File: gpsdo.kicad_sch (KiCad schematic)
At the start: 213 parts, among them J1 OLED, J10 10MHZ_OUT, J11 100MHZ_OUT, J12 10MHZ_OUT, J13 10MHZ_OUT, J14 10MHZ_OUT, J15 10MHZ_OUT, J16 LED, J17 TIMEPULSE, J18 USB_DM, J19 USB_DP, J2 ARDUINO_UART, J20 SDA, J21 SCL, J22 FREQ0, J23 BOOT, J24 RESET, J25 D_SEL, J26 Freq Out, J27 VCC_OUT, J28 VDD_USB, J29 V_ANT, J3 VOLTMETER, J4 ARDUINO_EXTRA_PINS, J5 POWER_IN, J6 GPS_ANT, J7 10MHZ_OUT, J8 10MHZ_OUT, J9 10MHZ_OUT, U1 TPS79301-EP, U10 MSA-0385, U11 MSA-0385, U12 MSA-0385, U13 MSA-0385, U14 MSA-0385, U15 MSA-0385, U16 MSA-0385, U17 MSA-0385, U18 MSA-0385, U19 MSA-0385, U2 TPS79301-EP, U20 MSA-0385, U21 TPS7A4501DCQT, U3 TPS7A4501DCQT, U4 SN74HC541DWR, U5 DAC8571IDGKR, U6 LEA-M8F, U7 CVSS-945, U8 SN74HC541DWR, U9 MC12080

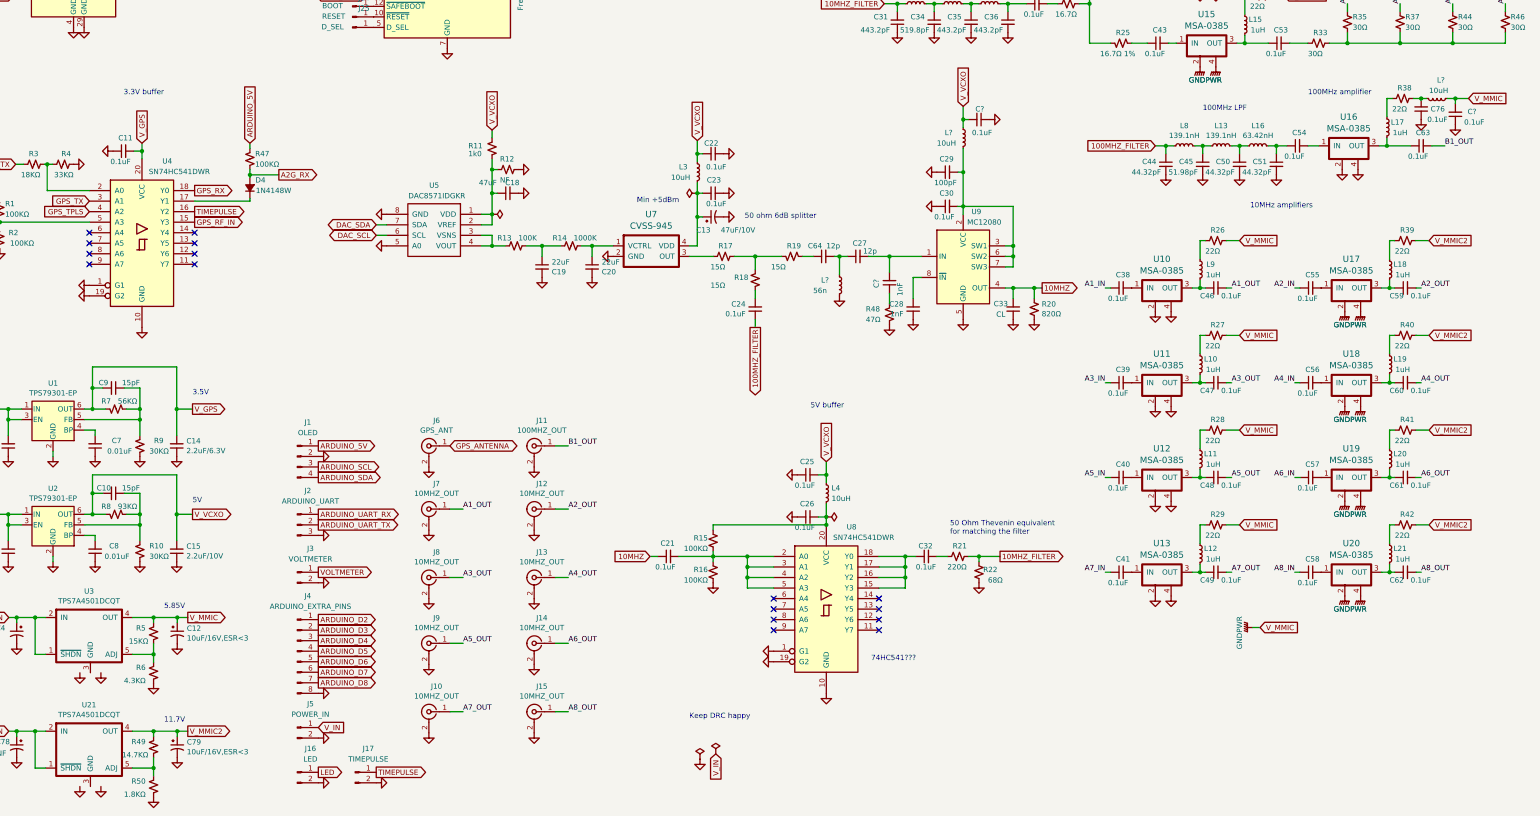
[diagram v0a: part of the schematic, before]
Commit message: Updated schematic references
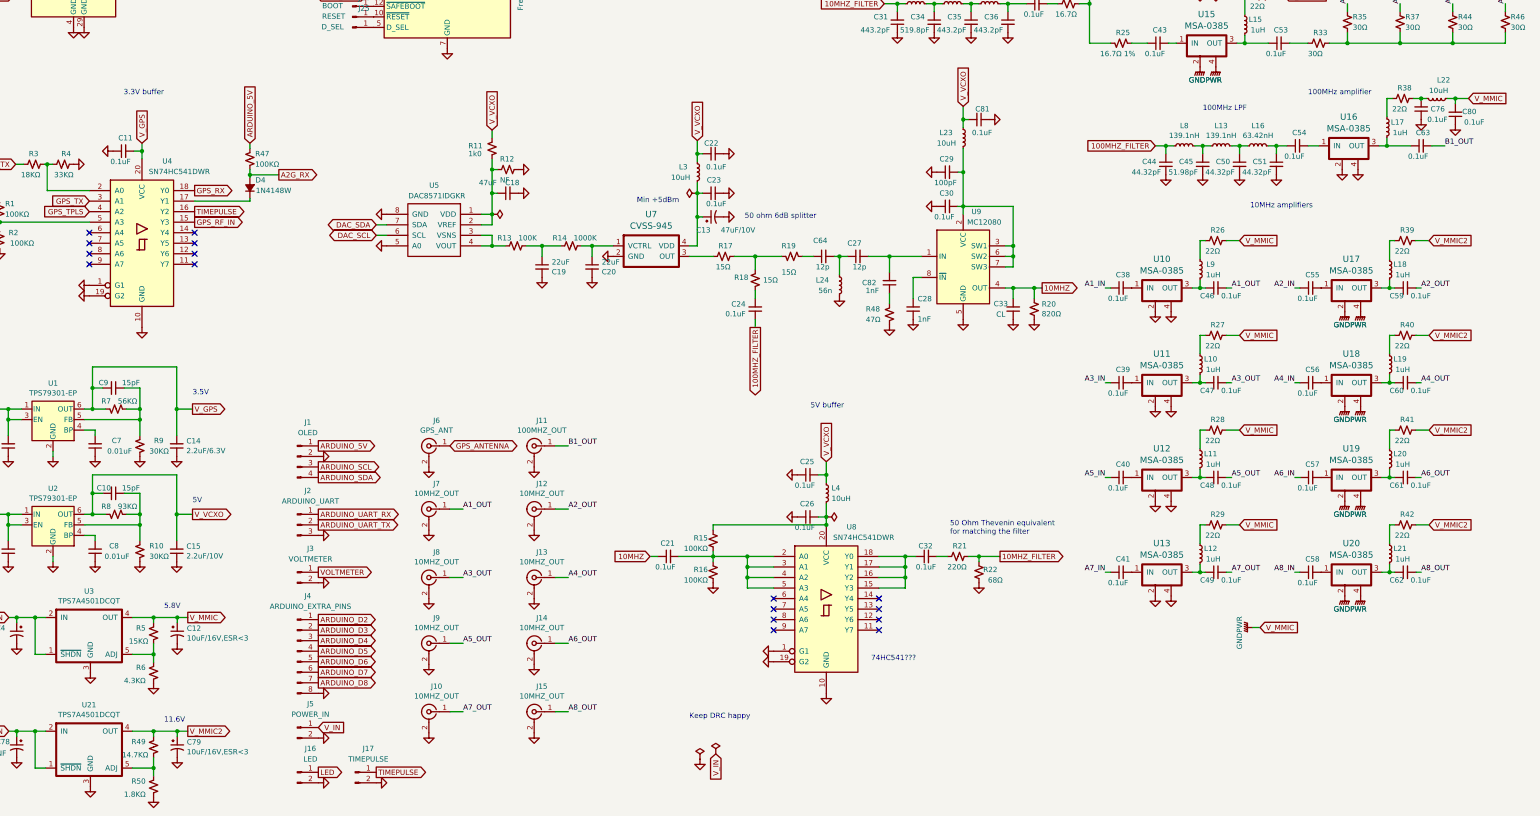
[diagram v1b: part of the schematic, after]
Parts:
- gave numbers to parts that had none: 6
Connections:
- net GND: now also U21.3 (GND), U3.3 (GND)
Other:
- note added: "11.6V"
- note added: "5.8V"
- note removed: "11.7V"
- note removed: "5.85V"
- moved on the sheet: C28
